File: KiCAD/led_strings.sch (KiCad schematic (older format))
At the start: 115 parts

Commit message: Update KiCAD files
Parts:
- added C6: EEE-FK1A102AL, Capacitor_SMD:CP_Elec_10x10, symbol Device:CP
- added U999: TL750M05CKTTR, Package_TO_SOT_SMD:TO-263-3_TabPin2, symbol Regulator_Current:HV100K5-G
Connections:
- net at LD0,0.1 (VDD), LD1,0.1 (VDD), LD10,0.1 (VDD)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: now also LD0,1.1 (VDD), LD0,2.1 (VDD), LD0,3.1 (VDD), LD0,4.1 (VDD), LD0,5.1 (VDD), LD1,1.1 (VDD), LD1,2.1 (VDD), LD1,3.1 (VDD), LD1,4.1 (VDD), LD1,5.1 (VDD), LD10,1.1 (VDD), LD10,2.1 (VDD), LD10,3.1 (VDD), LD10,4.1 (VDD), LD10,5.1 (VDD), LD11,1.1 (VDD), LD11,2.1 (VDD), LD11,3.1 (VDD), LD11,4.1 (VDD), LD11,5.1 (VDD), LD12,1.1 (VDD), LD12,2.1 (VDD), LD12,3.1 (VDD), LD13,1.1 (VDD), LD13,2.1 (VDD), LD14,1.1 (VDD), LD14,3.1 (VDD), LD14,6.1 (VDD), LD15,1.1 (VDD), LD15,3.1 (VDD), LD15,5.1 (VDD), LD15,6.1 (VDD), LD16,1.1 (VDD), LD16,3.1 (VDD), LD16,4.1 (VDD), LD16,5.1 (VDD), LD16,6.1 (VDD), LD17,1.1 (VDD), LD17,3.1 (VDD), LD17,4.1 (VDD), LD17,5.1 (VDD), LD17,6.1 (VDD), LD18,1.1 (VDD), LD18,3.1 (VDD), LD18,4.1 (VDD), LD18,5.1 (VDD), LD18,6.1 (VDD), LD19,1.1 (VDD), LD19,3.1 (VDD), LD19,4.1 (VDD), LD19,6.1 (VDD), LD2,1.1 (VDD), LD2,2.1 (VDD), LD2,3.1 (VDD), LD2,4.1 (VDD), LD2,5.1 (VDD), LD20,1.1 (VDD), LD20,4.1 (VDD), LD20,6.1 (VDD), LD3,1.1 (VDD), LD3,2.1 (VDD), LD3,3.1 (VDD), LD3,4.1 (VDD), LD3,5.1 (VDD), LD4,1.1 (VDD), LD4,2.1 (VDD), LD4,3.1 (VDD), LD4,4.1 (VDD), LD4,5.1 (VDD), LD5,1.1 (VDD), LD5,2.1 (VDD), LD5,3.1 (VDD), LD5,4.1 (VDD), LD5,5.1 (VDD), LD6,1.1 (VDD), LD6,2.1 (VDD), LD6,3.1 (VDD), LD6,4.1 (VDD), LD6,5.1 (VDD), LD7,1.1 (VDD), LD7,2.1 (VDD), LD7,3.1 (VDD), LD7,4.1 (VDD), LD7,5.1 (VDD), LD8,1.1 (VDD), LD8,2.1 (VDD), LD8,3.1 (VDD), LD8,4.1 (VDD), LD8,5.1 (VDD), LD9,1.1 (VDD), LD9,2.1 (VDD), LD9,3.1 (VDD), LD9,4.1 (VDD), LD9,5.1 (VDD), U999.3 (GATE)
- net GNDPWR: now reaches LD0,0.6 (GND), LD1,0.6 (GND), LD10,0.6 (GND), LD11,0.6 (GND), LD12,0.6 (GND), LD13,0.6 (GND), LD14,0.6 (GND), LD15,0.6 (GND), LD16,0.6 (GND), LD17,0.6 (GND), LD18,0.6 (GND), LD19,0.6 (GND), LD2,0.6 (GND), LD20,0.6 (GND), LD3,0.6 (GND), LD4,0.6 (GND), LD5,0.6 (GND), LD6,0.6 (GND), LD7,0.6 (GND), LD8,0.6 (GND), LD9,0.6 (GND)
- net GNDPWR: now also LD0,1.6 (GND), LD0,2.6 (GND), LD0,3.6 (GND), LD0,4.6 (GND), LD0,5.6 (GND), LD1,1.6 (GND), LD1,2.6 (GND), LD1,3.6 (GND), LD1,4.6 (GND), LD1,5.6 (GND), LD10,1.6 (GND), LD10,2.6 (GND), LD10,3.6 (GND), LD10,4.6 (GND), LD10,5.6 (GND), LD11,1.6 (GND), LD11,2.6 (GND), LD11,3.6 (GND), LD11,4.6 (GND), LD11,5.6 (GND), LD12,1.6 (GND), LD12,2.6 (GND), LD12,3.6 (GND), LD13,1.6 (GND), LD13,2.6 (GND), LD14,1.6 (GND), LD14,3.6 (GND), LD14,6.6 (GND), LD15,1.6 (GND), LD15,3.6 (GND), LD15,5.6 (GND), LD15,6.6 (GND), LD16,1.6 (GND), LD16,3.6 (GND), LD16,4.6 (GND), LD16,5.6 (GND), LD16,6.6 (GND), LD17,1.6 (GND), LD17,3.6 (GND), LD17,4.6 (GND), LD17,5.6 (GND), LD17,6.6 (GND), LD18,1.6 (GND), LD18,3.6 (GND), LD18,4.6 (GND), LD18,5.6 (GND), LD18,6.6 (GND), LD19,1.6 (GND), LD19,3.6 (GND), LD19,4.6 (GND), LD19,6.6 (GND), LD2,1.6 (GND), LD2,2.6 (GND), LD2,3.6 (GND), LD2,4.6 (GND), LD2,5.6 (GND), LD20,1.6 (GND), LD20,4.6 (GND), LD20,6.6 (GND), LD3,1.6 (GND), LD3,2.6 (GND), LD3,3.6 (GND), LD3,4.6 (GND), LD3,5.6 (GND), LD4,1.6 (GND), LD4,2.6 (GND), LD4,3.6 (GND), LD4,4.6 (GND), LD4,5.6 (GND), LD5,1.6 (GND), LD5,2.6 (GND), LD5,3.6 (GND), LD5,4.6 (GND), LD5,5.6 (GND), LD6,1.6 (GND), LD6,2.6 (GND), LD6,3.6 (GND), LD6,4.6 (GND), LD6,5.6 (GND), LD7,1.6 (GND), LD7,2.6 (GND), LD7,3.6 (GND), LD7,4.6 (GND), LD7,5.6 (GND), LD8,1.6 (GND), LD8,2.6 (GND), LD8,3.6 (GND), LD8,4.6 (GND), LD8,5.6 (GND), LD9,1.6 (GND), LD9,2.6 (GND), LD9,3.6 (GND), LD9,4.6 (GND), LD9,5.6 (GND), C6.2, U999.2 (VNN)
- new net MAIN_VBUS: C6.1, U999.1 (VPP)
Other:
- moved on the sheet: LD0,1, LD0,2, LD0,3, LD0,4, LD0,5, LD1,1, LD1,2, LD1,3, LD1,4, LD1,5, LD10,1, LD10,2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

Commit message: Update KiCAD files and README
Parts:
- added LD17,7, LD18,7, LD19,7, LD20,7: APA102-2020, CrumpPrints:APA102_hand_solder, symbol LED:APA102-2020
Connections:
- net GNDPWR: now also LD17,7.6 (GND), LD18,7.6 (GND), LD19,7.6 (GND), LD20,7.6 (GND)
- net at LD0,0.1 (VDD), LD0,1.1 (VDD), LD0,2.1 (VDD)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: now also LD17,7.1 (VDD), LD18,7.1 (VDD), LD19,7.1 (VDD), LD20,7.1 (VDD)
- new net: LD17,7.2 (CKO), LD18,7.5 (CKI)
- new net: LD17,7.3 (SDO), LD18,7.4 (SDI)
- new net: LD18,7.2 (CKO), LD19,7.5 (CKI)
- new net: LD18,7.3 (SDO), LD19,7.4 (SDI)
- new net: LD19,7.2 (CKO), LD20,7.5 (CKI)
- new net: LD19,7.3 (SDO), LD20,7.4 (SDI)
- new net LED_SCL_ROW7: LD17,7.5 (CKI)
- new net LED_SDA_ROW7: LD17,7.4 (SDI)
- no-connect marks 14 -> 16
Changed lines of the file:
@@
 	-1   0    0    1
 $EndComp
+$Comp
+L LED:APA102-2020 LD17,7
+U 1 1 6050EFF1
+P 6900 10550
+F 0 "LD17,7" H 6900 11031 50  0000 C CNN
+F 1 "APA102-2020" H 6900 10940 50  0000 C CNN
+F 2 "CrumpPrints:APA102_hand_solder" H 6950 10250 50  0001 L TNN
+F 3 "http://www.led-color.com/upload/201604/APA102-2020%20SMD%20LED.pdf" H 7000 10175 50  0001 L TNN
+	1    6900 10550
+	1    0    0    -1
+$EndComp
+Text GLabel 6600 10450 0    39   BiDi ~ 0
+LED_SDA_ROW7
+Text GLabel 6600 10550 0    39   BiDi ~ 0
+LED_SCL_ROW7
+Wire Wire Line
+	6900 10850 7500 10850
+Wire Wire Line
+	6900 10250 7500 10250
+$Comp
+L LED:APA102-2020 LD18,7
+U 1 1 6050EFFB
+P 7500 10550
+F 0 "LD18,7" H 7500 11031 50  0000 C CNN
+F 1 "APA102-2020" H 7500 10940 50  0000 C CNN
+F 2 "CrumpPrints:APA102_hand_solder" H 7550 10250 50  0001 L TNN
+F 3 "http://www.led-color.com/upload/201604/APA102-2020%20SMD%20LED.pdf" H 7600 10175 50  0001 L TNN
+	1    7500 10550
+	1    0    0    -1
+$EndComp
+Wire Wire Line
+	7500 10850 8100 10850
+Wire Wire Line
+	7500 10250 8100 10250
+$Comp
+L LED:APA102-2020 LD19,7
+U 1 1 6050F003
+P 8100 10550
+F 0 "LD19,7" H 8100 11031 50  0000 C CNN
+F 1 "APA102-2020" H 8100 10940 50  0000 C CNN
+F 2 "CrumpPrints:APA102_hand_solder" H 8150 10250 50  0001 L TNN
+F 3 "http://www.led-color.com/upload/201604/APA102-2020%20SMD%20LED.pdf" H 8200 10175 50  0001 L TNN
+	1    8100 10550
+	1    0    0    -1
+$EndComp
+Connection ~ 7500 10250
+Connection ~ 7500 10850
+Connection ~ 8100 10250
+Connection ~ 8100 10850
+Wire Wire Line
+	8100 10850 8700 10850
+$Comp
+L LED:APA102-2020 LD20,7
+U 1 1 6050F00B
+P 8700 10550
+F 0 "LD20,7" H 8700 11031 50  0000 C CNN
+F 1 "APA102-2020" H 8700 10940 50  0000 C CNN
+F 2 "CrumpPrints:APA102_hand_solder" H 8750 10250 50  0001 L TNN
+F 3 "http://www.led-color.com/upload/201604/APA102-2020%20SMD%20LED.pdf" H 8800 10175 50  0001 L TNN
+	1    8700 10550
+	1    0    0    -1
+$EndComp
+NoConn ~ 9000 10450
+NoConn ~ 9000 10550
+Wire Wire Line
+	9650 10250 9650 9900
+Wire Wire Line
+	9650 9900 12850 9900
+Connection ~ 12850 9900
+$Comp
+L power:GNDPWR #PWR?
+U 1 1 606F9755
+P 8700 10850
+F 0 "#PWR?" H 8700 10650 50  0001 C CNN
+F 1 "GNDPWR" V 8705 10742 50  0000 R CNN
+F 2 "" H 8700 10800 50  0001 C CNN
+F 3 "" H 8700 10800 50  0001 C CNN
+	1    8700 10850
+	0    -1   -1   0
+$EndComp
+Wire Wire Line
+	8100 10250 8700 10250
+Connection ~ 8700 10250
+Wire Wire Line
+	8700 10250 9650 10250
+Connection ~ 8700 10850
+Connection ~ 14350 10850
+Connection ~ 13250 9500
+Connection ~ 14200 8000
+Connection ~ 13550 6350
+Connection ~ 9900 4700
+Connection ~ 14100 3400
+Connection ~ 14150 1750
 $EndSCHEMATC

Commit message: Update KiCAD files
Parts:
- removed U999: TL750M05CKTTR, Package_TO_SOT_SMD:TO-263-3_TabPin2, symbol Regulator_Current:HV100K5-G
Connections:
- net MAIN_VBUS: now also LD0,0.1 (VDD), LD0,1.1 (VDD), LD0,2.1 (VDD), LD0,3.1 (VDD), LD0,4.1 (VDD), LD0,5.1 (VDD), LD1,0.1 (VDD), LD1,1.1 (VDD), LD1,2.1 (VDD), LD1,3.1 (VDD), LD1,4.1 (VDD), LD1,5.1 (VDD), LD10,0.1 (VDD), LD10,1.1 (VDD), LD10,2.1 (VDD), LD10,3.1 (VDD), LD10,4.1 (VDD), LD10,5.1 (VDD), LD11,0.1 (VDD), LD11,1.1 (VDD), LD11,2.1 (VDD), LD11,3.1 (VDD), LD11,4.1 (VDD), LD11,5.1 (VDD), LD12,0.1 (VDD), LD12,1.1 (VDD), LD12,2.1 (VDD), LD12,3.1 (VDD), LD13,0.1 (VDD), LD13,1.1 (VDD), LD13,2.1 (VDD), LD14,0.1 (VDD), LD14,1.1 (VDD), LD14,3.1 (VDD), LD14,6.1 (VDD), LD15,0.1 (VDD), LD15,1.1 (VDD), LD15,3.1 (VDD), LD15,5.1 (VDD), LD15,6.1 (VDD), LD16,0.1 (VDD), LD16,1.1 (VDD), LD16,3.1 (VDD), LD16,4.1 (VDD), LD16,5.1 (VDD), LD16,6.1 (VDD), LD17,0.1 (VDD), LD17,1.1 (VDD), LD17,3.1 (VDD), LD17,4.1 (VDD), LD17,5.1 (VDD), LD17,6.1 (VDD), LD17,7.1 (VDD), LD18,0.1 (VDD), LD18,1.1 (VDD), LD18,3.1 (VDD), LD18,4.1 (VDD), LD18,5.1 (VDD), LD18,6.1 (VDD), LD18,7.1 (VDD), LD19,0.1 (VDD), LD19,1.1 (VDD), LD19,3.1 (VDD), LD19,4.1 (VDD), LD19,6.1 (VDD), LD19,7.1 (VDD), LD2,0.1 (VDD), LD2,1.1 (VDD), LD2,2.1 (VDD), LD2,3.1 (VDD), LD2,4.1 (VDD), LD2,5.1 (VDD), LD20,0.1 (VDD), LD20,1.1 (VDD), LD20,4.1 (VDD), LD20,6.1 (VDD), LD20,7.1 (VDD), LD3,0.1 (VDD), LD3,1.1 (VDD), LD3,2.1 (VDD), LD3,3.1 (VDD), LD3,4.1 (VDD), LD3,5.1 (VDD), LD4,0.1 (VDD), LD4,1.1 (VDD), LD4,2.1 (VDD), LD4,3.1 (VDD), LD4,4.1 (VDD), LD4,5.1 (VDD), LD5,0.1 (VDD), LD5,1.1 (VDD), LD5,2.1 (VDD), LD5,3.1 (VDD), LD5,4.1 (VDD), LD5,5.1 (VDD), LD6,0.1 (VDD), LD6,1.1 (VDD), LD6,2.1 (VDD), LD6,3.1 (VDD), LD6,4.1 (VDD), LD6,5.1 (VDD), LD7,0.1 (VDD), LD7,1.1 (VDD), LD7,2.1 (VDD), LD7,3.1 (VDD), LD7,4.1 (VDD), LD7,5.1 (VDD), LD8,0.1 (VDD), LD8,1.1 (VDD), LD8,2.1 (VDD), LD8,3.1 (VDD), LD8,4.1 (VDD), LD8,5.1 (VDD), LD9,0.1 (VDD), LD9,1.1 (VDD), LD9,2.1 (VDD), LD9,3.1 (VDD), LD9,4.1 (VDD), LD9,5.1 (VDD)
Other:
- moved on the sheet: C6
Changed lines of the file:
@@
 L power:GNDPWR #PWR0115
 U 1 1 64AC578A
-P 16350 5700
-F 0 "#PWR0115" H 16350 5500 50  0001 C CNN
-F 1 "GNDPWR" V 16354 5591 50  0000 R CNN
-F 2 "" H 16350 5650 50  0001 C CNN
-F 3 "" H 16350 5650 50  0001 C CNN
-	1    16350 5700
+P 16050 5100
+F 0 "#PWR0115" H 16050 4900 50  0001 C CNN
+F 1 "GNDPWR" V 16054 4991 50  0000 R CNN
+F 2 "" H 16050 5050 50  0001 C CNN
+F 3 "" H 16050 5050 50  0001 C CNN
+	1    16050 5100
 	-1   0    0    1
 $EndComp
-Text GLabel 16350 6000 3    39   BiDi ~ 0
+Text GLabel 16050 5400 3    39   BiDi ~ 0
 MAIN_VBUS
 Wire Wire Line
-	16350 5700 16200 5700
-Wire Wire Line
-	16200 6000 16350 6000
+	16050 5100 15900 5100
+Wire Wire Line
+	15900 5400 16050 5400
 $Comp
 L Device:CP C?
 U 1 1 64B87B14
-P 16200 5850
+P 15900 5250
 AR Path="/64B87B14" Ref="C?"  Part="1"
 AR Path="/63412601/64B87B14" Ref="C6"  Part="1"
-F 0 "C6" V 16455 5850 50  0000 C CNN
-F 1 "EEE-FK1A102AL" V 16364 5850 50  0000 C CNN
-F 2 "Capacitor_SMD:CP_Elec_10x10" H 16238 5700 50  0001 C CNN
-F 3 "~" H 16200 5850 50  0001 C CNN
-	1    16200 5850
+F 0 "C6" V 16155 5250 50  0000 C CNN
+F 1 "EEE-FK1A102AL" V 16064 5250 50  0000 C CNN
+F 2 "Capacitor_SMD:CP_Elec_10x10" H 15938 5100 50  0001 C CNN
+F 3 "~" H 15900 5250 50  0001 C CNN
+	1    15900 5250
 	-1   0    0    1
 $EndComp
@@
 Wire Wire Line
 	9900 5400 15300 5400
-$Comp
-L Regulator_Current:HV100K5-G U999
-U 1 1 651D72E7
-P 15600 5400
-F 0 "U999" H 15370 5354 50  0000 R CNN
-F 1 "TL750M05CKTTR" H 15370 5445 50  0000 R CNN
-F 2 "Package_TO_SOT_SMD:TO-263-3_TabPin2" H 15600 4900 50  0001 C CNN
-F 3 "" H 15950 5450 50  0001 C CNN
-	1    15600 5400
-	-1   0    0    1
-$EndComp
-Wire Wire Line
-	16200 6000 15600 6000
-Wire Wire Line
-	15600 6000 15600 5800
-Connection ~ 16200 6000
-Wire Wire Line
-	15600 5000 15600 4800
-Wire Wire Line
-	15600 4800 15750 4800
-$Comp
-L power:GNDPWR #PWR?
-U 1 1 6526ED2F
-P 15750 4800
-F 0 "#PWR?" H 15750 4600 50  0001 C CNN
-F 1 "GNDPWR" V 15754 4691 50  0000 R CNN
-F 2 "" H 15750 4750 50  0001 C CNN
-F 3 "" H 15750 4750 50  0001 C CNN
-	1    15750 4800
-	-1   0    0    1
-$EndComp
+Wire Wire Line
+	15900 5400 15300 5400
+Connection ~ 15900 5400
 $Comp
 L LED:APA102-2020 LD17,7

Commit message: Update KiCAD files
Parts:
- removed LD13,0, LD20,4, LD20,6, LD4,5, LD5,5, LD6,5, LD7,5: APA102-2020, CrumpPrints:APA102_hand_solder, symbol LED:APA102-2020
- LD0,0, LD0,1, LD0,2, LD0,3, LD0,4, LD0,5, LD1,0, LD1,1, LD1,2, LD1,3, LD1,4, LD1,5, LD10,0, LD10,1, LD10,2, LD10,3, LD10,4, LD10,5, LD11,0, LD11,1, LD11,2, LD11,3, LD11,4, LD11,5, LD12,0, LD12,1, LD12,2, LD12,3, LD13,1, LD13,2, LD14,0, LD14,1, LD14,3, LD14,6, LD15,0, LD15,1, LD15,3, LD15,5, LD15,6, LD16,0, LD16,1, LD16,3, LD16,4, LD16,5, LD16,6, LD17,0, LD17,1, LD17,3, LD17,4, LD17,5, LD17,6, LD17,7, LD18,0, LD18,1, LD18,3, LD18,4, LD18,5, LD18,6, LD18,7, LD19,0, LD19,1, LD19,3, LD19,4, LD19,6, LD19,7, LD2,0, LD2,1, LD2,2, LD2,3, LD2,4, LD2,5, LD20,0, LD20,1, LD20,7, LD3,0, LD3,1, LD3,2, LD3,3, LD3,4, LD3,5, LD4,0, LD4,1, LD4,2, LD4,3, LD4,4, LD5,0, LD5,1, LD5,2, LD5,3, LD5,4, LD6,0, LD6,1, LD6,2, LD6,3, LD6,4, LD7,0, LD7,1, LD7,2, LD7,3, LD7,4, LD8,0, LD8,1, LD8,2, LD8,3, LD8,4, LD8,5, LD9,0, LD9,1, LD9,2, LD9,3, LD9,4, LD9,5: footprint CrumpPrints:APA102_hand_solder -> Custom_pico:LED-APA102-2020
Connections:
- net at LD12,0.2 (CKO): now also LD14,0.5 (CKI)
- net at LD12,0.3 (SDO): now also LD14,0.4 (SDI)
- net at LD3,5.2 (CKO): now also LD8,5.5 (CKI)
- net at LD3,5.3 (SDO): now also LD8,5.4 (SDI)

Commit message: Update KiCAD files
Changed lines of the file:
@@
 	-1   0    0    1
 $EndComp
-Text GLabel 16050 5400 3    39   BiDi ~ 0
+Text GLabel 16050 5400 3    39   Input ~ 0
 MAIN_VBUS
 Wire Wire Line

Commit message: Update KiCAD files.
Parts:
- C6: value EEE-FK1A102AL -> EEE-FN1C102UV; Mouser No (none) -> 667-EEE-FN1C102UV
- LD0,0, LD0,1, LD0,2, LD0,3, LD0,4, LD0,5, LD1,0, LD1,1, LD1,2, LD1,3, LD1,4, LD1,5, LD10,0, LD10,1, LD10,2, LD10,3, LD10,4, LD10,5, LD11,0, LD11,1, LD11,2, LD11,3, LD11,4, LD11,5, LD12,0, LD12,1, LD12,2, LD12,3, LD13,1, LD13,2, LD14,0, LD14,1, LD14,3, LD14,6, LD15,0, LD15,1, LD15,3, LD15,5, LD15,6, LD16,0, LD16,1, LD16,3, LD16,4, LD16,5, LD16,6, LD17,0, LD17,1, LD17,3, LD17,4, LD17,5, LD17,6, LD17,7, LD18,0, LD18,1, LD18,3, LD18,4, LD18,5, LD18,6, LD18,7, LD19,0, LD19,1, LD19,3, LD19,4, LD19,6, LD19,7, LD2,0, LD2,1, LD2,2, LD2,3, LD2,4, LD2,5, LD20,0, LD20,1, LD20,7, LD3,0, LD3,1, LD3,2, LD3,3, LD3,4, LD3,5, LD4,0, LD4,1, LD4,2, LD4,3, LD4,4, LD5,0, LD5,1, LD5,2, LD5,3, LD5,4, LD6,0, LD6,1, LD6,2, LD6,3, LD6,4, LD7,0, LD7,1, LD7,2, LD7,3, LD7,4, LD8,0, LD8,1, LD8,2, LD8,3, LD8,4, LD8,5, LD9,0, LD9,1, LD9,2, LD9,3, LD9,4, LD9,5: value APA102-2020 -> APA102 2020; Mouser No (none) -> 485-3587

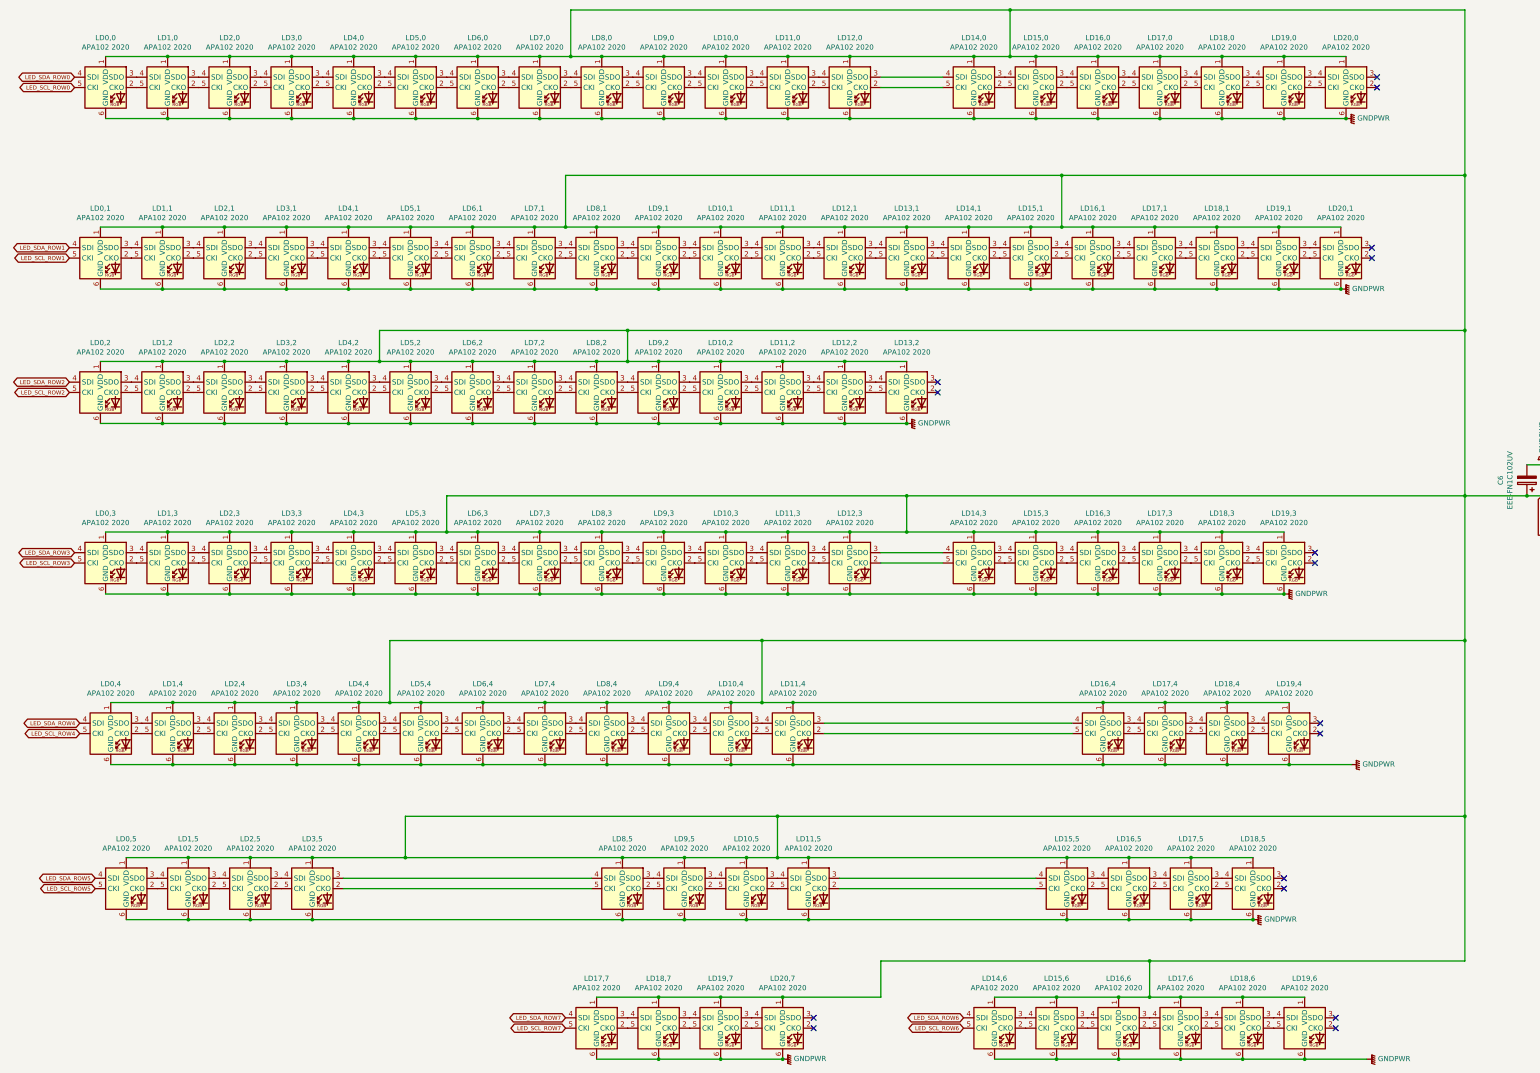
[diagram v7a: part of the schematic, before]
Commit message: KiCAD and firmware updates, first working firmware and half way through a board rewire after the initial semi-working board. Firmware has no real LED control other than the power budget system and pin setup. Although the firmware works, it is not a working keyboard, yet.
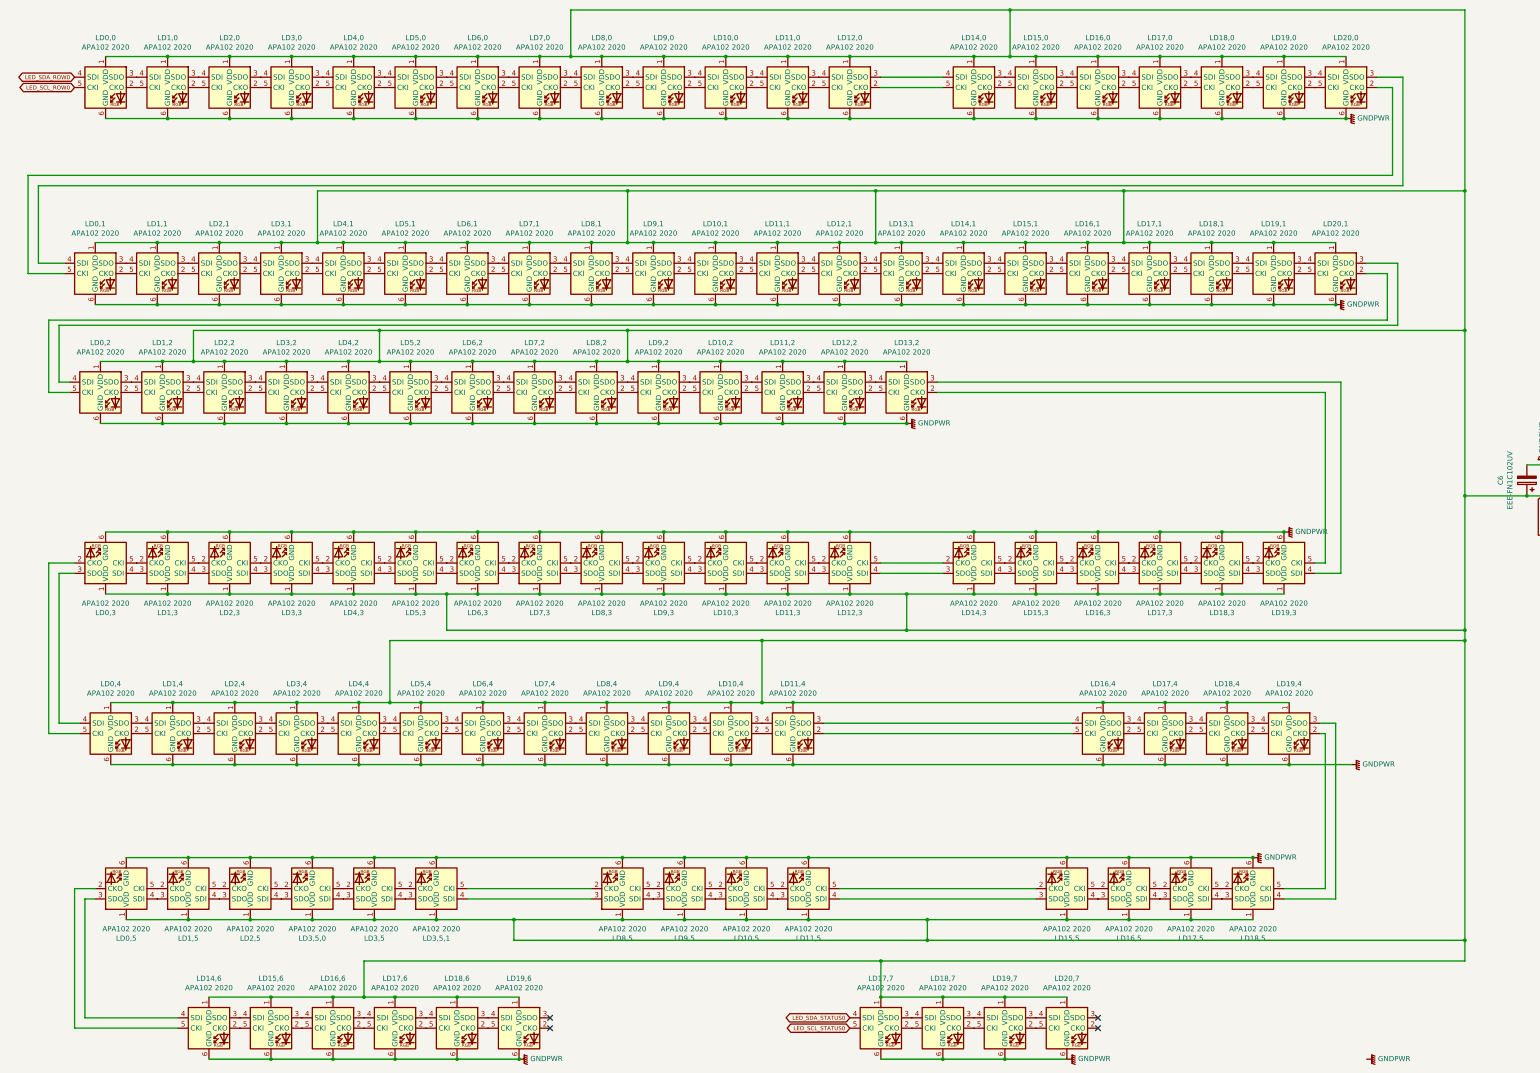
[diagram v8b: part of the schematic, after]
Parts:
- added LD3,5,0, LD3,5,1: APA102 2020, Custom_pico:LED-APA102-2020, symbol LED:APA102-2020
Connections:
- net LED_SCL_ROW1 is gone; now on an unnamed net: LD0,1.5 (CKI)
- net LED_SCL_ROW2 is gone; now on an unnamed net: LD0,2.5 (CKI)
- net LED_SCL_ROW3 is gone; now on an unnamed net: LD0,3.5 (CKI)
- net LED_SCL_ROW4 is gone; now on an unnamed net: LD0,4.5 (CKI)
- net LED_SCL_ROW6 is gone; now on an unnamed net: LD14,6.5 (CKI)
- net LED_SDA_ROW1 is gone; now on an unnamed net: LD0,1.4 (SDI)
- net LED_SDA_ROW2 is gone; now on an unnamed net: LD0,2.4 (SDI)
- net LED_SDA_ROW3 is gone; now on an unnamed net: LD0,3.4 (SDI)
- net LED_SDA_ROW4 is gone; now on an unnamed net: LD0,4.4 (SDI)
- net LED_SDA_ROW6 is gone; now on an unnamed net: LD14,6.4 (SDI)
- net GNDPWR: now also LD3,5,0.6 (GND), LD3,5,1.6 (GND)
- net MAIN_VBUS: now also LD3,5,0.1 (VDD), LD3,5,1.1 (VDD)
- net at LD13,2.2 (CKO): now also LD19,3.5 (CKI)
- net at LD13,2.3 (SDO): now also LD19,3.4 (SDI)
- net at LD0,3.2 (CKO): no longer LD1,3.5 (CKI)
- net at LD0,3.3 (SDO): no longer LD1,3.4 (SDI)
- net at LD1,3.2 (CKO): no longer LD2,3.5 (CKI)
- net at LD1,3.3 (SDO): no longer LD2,3.4 (SDI)
- net at LD2,3.2 (CKO): now also LD1,3.5 (CKI); no longer LD3,3.5 (CKI)
- net at LD2,3.3 (SDO): now also LD1,3.4 (SDI); no longer LD3,3.4 (SDI)
- net at LD3,3.2 (CKO): now also LD2,3.5 (CKI); no longer LD4,3.5 (CKI)
- net at LD3,3.3 (SDO): now also LD2,3.4 (SDI); no longer LD4,3.4 (SDI)
- net at LD4,3.2 (CKO): now also LD3,3.5 (CKI); no longer LD5,3.5 (CKI)
- net at LD4,3.3 (SDO): now also LD3,3.4 (SDI); no longer LD5,3.4 (SDI)
- net at LD5,3.2 (CKO): now also LD4,3.5 (CKI); no longer LD6,3.5 (CKI)
- net at LD5,3.3 (SDO): now also LD4,3.4 (SDI); no longer LD6,3.4 (SDI)
- net at LD6,3.2 (CKO): now also LD5,3.5 (CKI); no longer LD7,3.5 (CKI)
- net at LD6,3.3 (SDO): now also LD5,3.4 (SDI); no longer LD7,3.4 (SDI)
- net at LD7,3.2 (CKO): now also LD6,3.5 (CKI); no longer LD8,3.5 (CKI)
- net at LD7,3.3 (SDO): now also LD6,3.4 (SDI); no longer LD8,3.4 (SDI)
- net at LD8,3.2 (CKO): now also LD7,3.5 (CKI); no longer LD9,3.5 (CKI)
- net at LD8,3.3 (SDO): now also LD7,3.4 (SDI); no longer LD9,3.4 (SDI)
- net at LD9,3.2 (CKO): now also LD8,3.5 (CKI); no longer LD10,3.5 (CKI)
- net at LD9,3.3 (SDO): now also LD8,3.4 (SDI); no longer LD10,3.4 (SDI)
- net at LD10,3.2 (CKO): now also LD9,3.5 (CKI); no longer LD11,3.5 (CKI)
- net at LD10,3.3 (SDO): now also LD9,3.4 (SDI); no longer LD11,3.4 (SDI)
- net at LD11,3.2 (CKO): now also LD10,3.5 (CKI); no longer LD12,3.5 (CKI)
- net at LD11,3.3 (SDO): now also LD10,3.4 (SDI); no longer LD12,3.4 (SDI)
- net at LD12,3.2 (CKO): now also LD11,3.5 (CKI); no longer LD14,3.5 (CKI)
- net at LD12,3.3 (SDO): now also LD11,3.4 (SDI); no longer LD14,3.4 (SDI)
- net at LD14,3.2 (CKO): now also LD12,3.5 (CKI); no longer LD15,3.5 (CKI)
- net at LD14,3.3 (SDO): now also LD12,3.4 (SDI); no longer LD15,3.4 (SDI)
- net at LD15,3.2 (CKO): now also LD14,3.5 (CKI); no longer LD16,3.5 (CKI)
- net at LD15,3.3 (SDO): now also LD14,3.4 (SDI); no longer LD16,3.4 (SDI)
- net at LD16,3.2 (CKO): now also LD15,3.5 (CKI); no longer LD17,3.5 (CKI)
- net at LD16,3.3 (SDO): now also LD15,3.4 (SDI); no longer LD17,3.4 (SDI)
- net at LD17,3.2 (CKO): now also LD16,3.5 (CKI); no longer LD18,3.5 (CKI)
- net at LD17,3.3 (SDO): now also LD16,3.4 (SDI); no longer LD18,3.4 (SDI)
- net at LD18,3.2 (CKO): now also LD17,3.5 (CKI); no longer LD19,3.5 (CKI)
- net at LD18,3.3 (SDO): now also LD17,3.4 (SDI); no longer LD19,3.4 (SDI)
- net at LD19,3.2 (CKO): now also LD18,3.5 (CKI)
- net at LD19,3.3 (SDO): now also LD18,3.4 (SDI)
- net at LD19,4.2 (CKO): now also LD18,5.5 (CKI)
- net at LD19,4.3 (SDO): now also LD18,5.4 (SDI)
- net at LD0,5.2 (CKO): no longer LD1,5.5 (CKI)
- net at LD0,5.3 (SDO): no longer LD1,5.4 (SDI)
- net at LD2,5.5 (CKI): now also LD3,5,0.2 (CKO); no longer LD1,5.2 (CKO)
- net at LD2,5.4 (SDI): now also LD3,5,0.3 (SDO); no longer LD1,5.3 (SDO)
- net at LD3,5.5 (CKI): now also LD3,5,1.2 (CKO); no longer LD2,5.2 (CKO)
- net at LD3,5.4 (SDI): now also LD3,5,1.3 (SDO); no longer LD2,5.3 (SDO)
- net at LD3,5.2 (CKO): now also LD3,5,0.5 (CKI); no longer LD8,5.5 (CKI)
- net at LD3,5.3 (SDO): now also LD3,5,0.4 (SDI); no longer LD8,5.4 (SDI)
- net at LD8,5.2 (CKO): now also LD3,5,1.5 (CKI); no longer LD9,5.5 (CKI)
- net at LD8,5.3 (SDO): now also LD3,5,1.4 (SDI); no longer LD9,5.4 (SDI)
- net at LD9,5.2 (CKO): now also LD8,5.5 (CKI); no longer LD10,5.5 (CKI)
- net at LD9,5.3 (SDO): now also LD8,5.4 (SDI); no longer LD10,5.4 (SDI)
- net at LD10,5.2 (CKO): now also LD9,5.5 (CKI); no longer LD11,5.5 (CKI)
- net at LD10,5.3 (SDO): now also LD9,5.4 (SDI); no longer LD11,5.4 (SDI)
- net at LD11,5.2 (CKO): now also LD10,5.5 (CKI); no longer LD15,5.5 (CKI)
- net at LD11,5.3 (SDO): now also LD10,5.4 (SDI); no longer LD15,5.4 (SDI)
- net at LD15,5.2 (CKO): now also LD11,5.5 (CKI); no longer LD16,5.5 (CKI)
- net at LD15,5.3 (SDO): now also LD11,5.4 (SDI); no longer LD16,5.4 (SDI)
- net at LD16,5.2 (CKO): now also LD15,5.5 (CKI); no longer LD17,5.5 (CKI)
- net at LD16,5.3 (SDO): now also LD15,5.4 (SDI); no longer LD17,5.4 (SDI)
- net at LD17,5.2 (CKO): now also LD16,5.5 (CKI); no longer LD18,5.5 (CKI)
- net at LD17,5.3 (SDO): now also LD16,5.4 (SDI); no longer LD18,5.4 (SDI)
- net at LD18,5.2 (CKO): now also LD17,5.5 (CKI)
- net at LD18,5.3 (SDO): now also LD17,5.4 (SDI)
- net LED_SCL_ROW5: no longer names the net of LD0,5.5 (CKI)
- net LED_SCL_ROW5: now also LD1,5.2 (CKO)
- net LED_SCL_ROW7 renamed LED_SCL_STATUS0
- net LED_SDA_ROW5: no longer names the net of LD0,5.4 (SDI)
- net LED_SDA_ROW5: now also LD1,5.3 (SDO)
- net LED_SDA_ROW7 renamed LED_SDA_STATUS0
- new net: LD1,5.4 (SDI), LD2,5.3 (SDO)
- new net: LD1,5.5 (CKI), LD2,5.2 (CKO)
- no-connect marks 16 -> 4
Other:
- moved on the sheet: LD0,1, LD1,1, LD10,1, LD11,1, LD12,1, LD13,1, LD14,1, LD14,6, LD15,1, LD15,6, LD16,1, LD16,6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
